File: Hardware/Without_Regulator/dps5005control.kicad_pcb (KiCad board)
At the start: 2 copper layers, 50 x 53.5 mm, 24 parts, among them P1 CONN_01X07, P2 CONN_4, P3 CONN_5X2, P4 CONN_7, U2 ATTINY2313-20PU

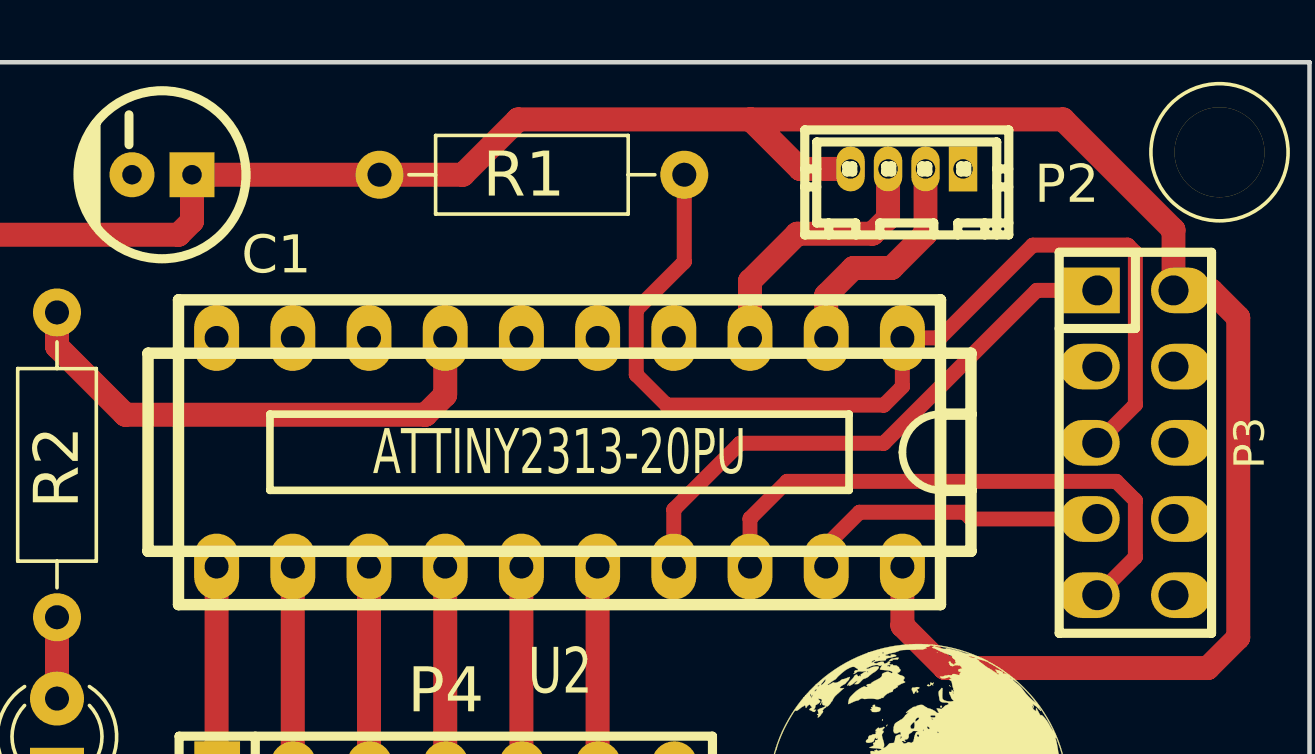
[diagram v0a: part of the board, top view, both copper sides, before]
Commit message: HARD: Swapped P2 with R1 in the version without regulator.
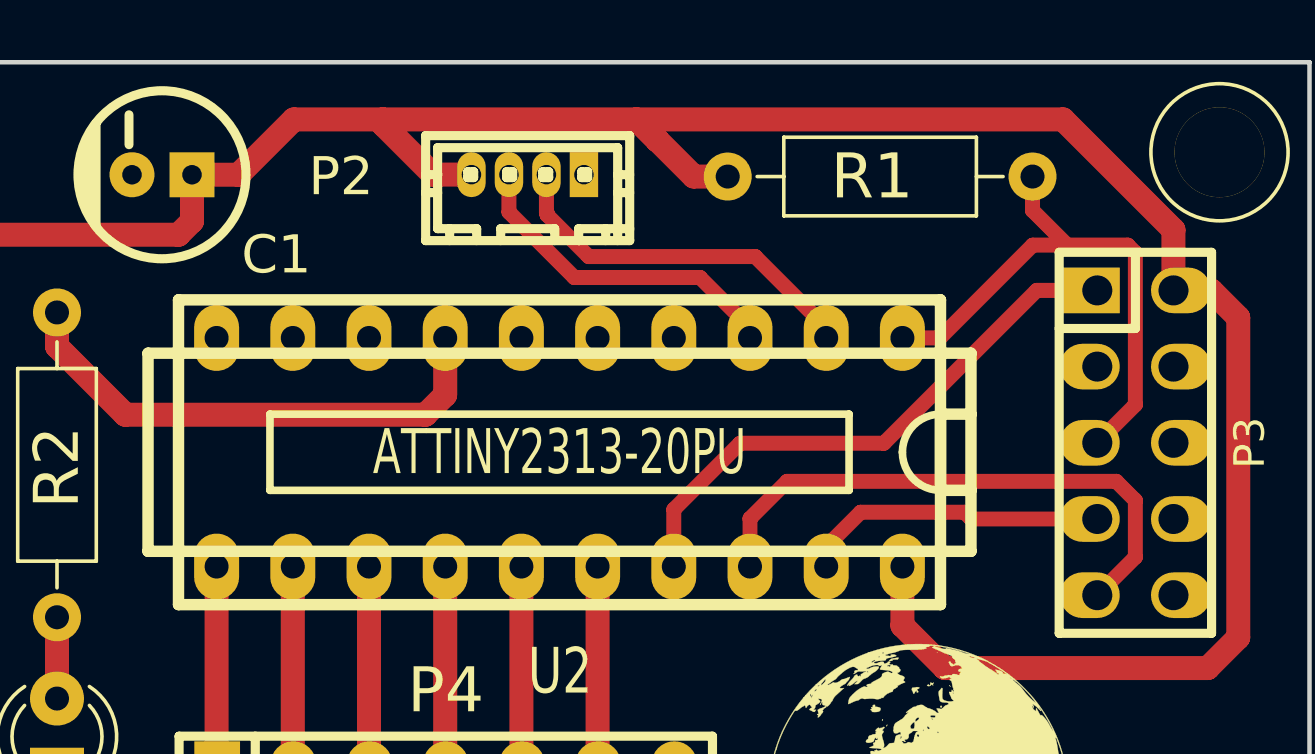
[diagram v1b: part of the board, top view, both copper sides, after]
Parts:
- moved P2 12.6 mm to (176.3, 67.9)
- moved R1 11.6 mm to (183.0, 68.0)
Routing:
- net /RST: track 34.5 -> 18.8 mm
- net /Rx: track 7.75 -> 12.6 mm
- net +3.3V: track 80.7 -> 84.4 mm
- net /Tx: track 9.28 -> 11.2 mm
